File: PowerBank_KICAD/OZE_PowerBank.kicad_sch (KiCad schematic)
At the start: 62 parts, among them IC1 TPS2514ADBVT, J2 Conn_01x04_Pin, J3 USB_C_Receptacle_PowerOnly_6P, J4 USB_B_Micro, J5 Conn_01x04_Pin, J6 Conn_01x04_Pin, P1 USB_C_Plug_USB2.0, Q1 IRLZ44N, Q2 IRLZ44N, SW1 SW_SPDT, SW2 SW_Push, U1 INA180A2, U1 LM5106SD, U2 TLV70233_SOT23-5, U3 TPS25810RVCR, U4 STM32F103C8Tx, Y1 16MHz

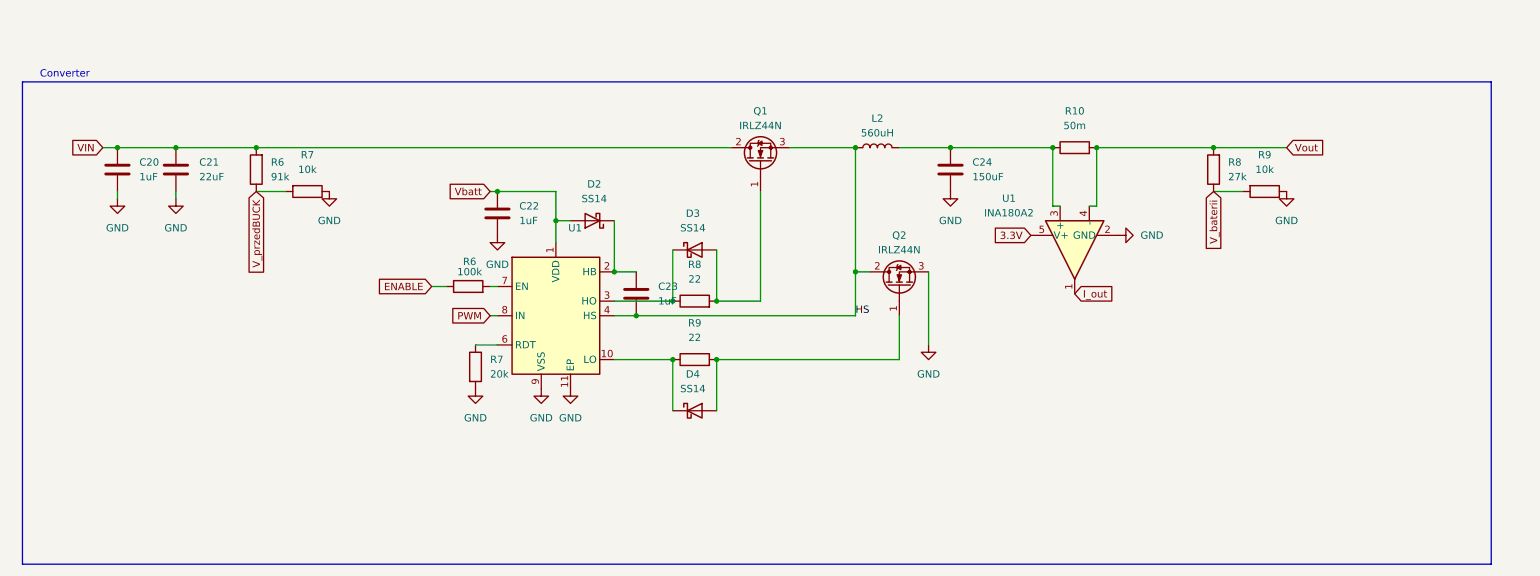
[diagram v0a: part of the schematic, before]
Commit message: 04.11
- 150uF kondensatory to elektrolity ważny LOW RMS!
- Przetwornica do sterownika (IMZ Przetwornica MT3608 2A Step-Up DC/DC) gotowa płytka
- 100 kHz sterowanie PWM (tak dobrany jest dławik i kondensatory co widać na symulacji)

Symulacja w LT Spice
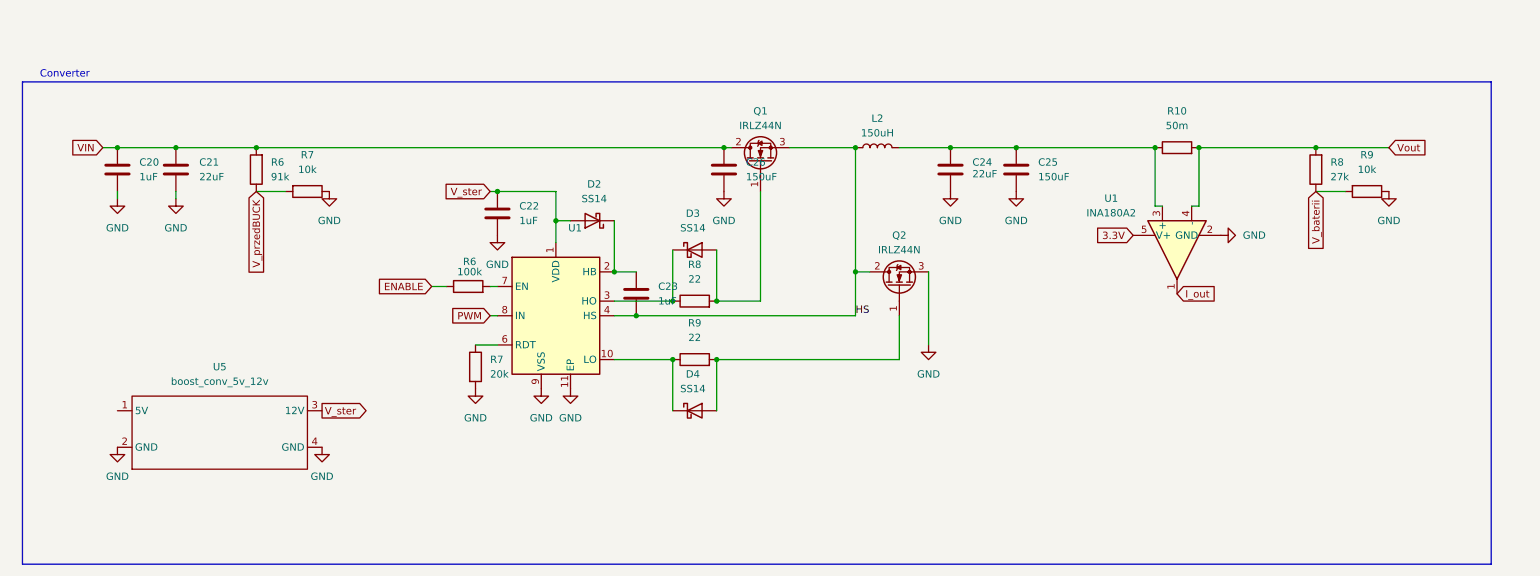
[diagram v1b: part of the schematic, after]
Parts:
- added C25, C26: 150uF, symbol Device:C
- added U5: boost_conv_5v_12v, symbol Biblioteka_PowerBank:boost_conv_5v_12v
- C24: value 150uF -> 22uF
- L2: value 560uH -> 150uH
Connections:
- net GND: now also C25.2, C26.2, U5.2 (GND), U5.4 (GND)
- net VIN: now also C26.1
- net at C24.1, L2.2, R10.1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: now also C25.1
- net Vbatt renamed V_ster
- net V_ster: now also U5.3 (12V)
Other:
- moved on the sheet: R10, R8, R9, U1

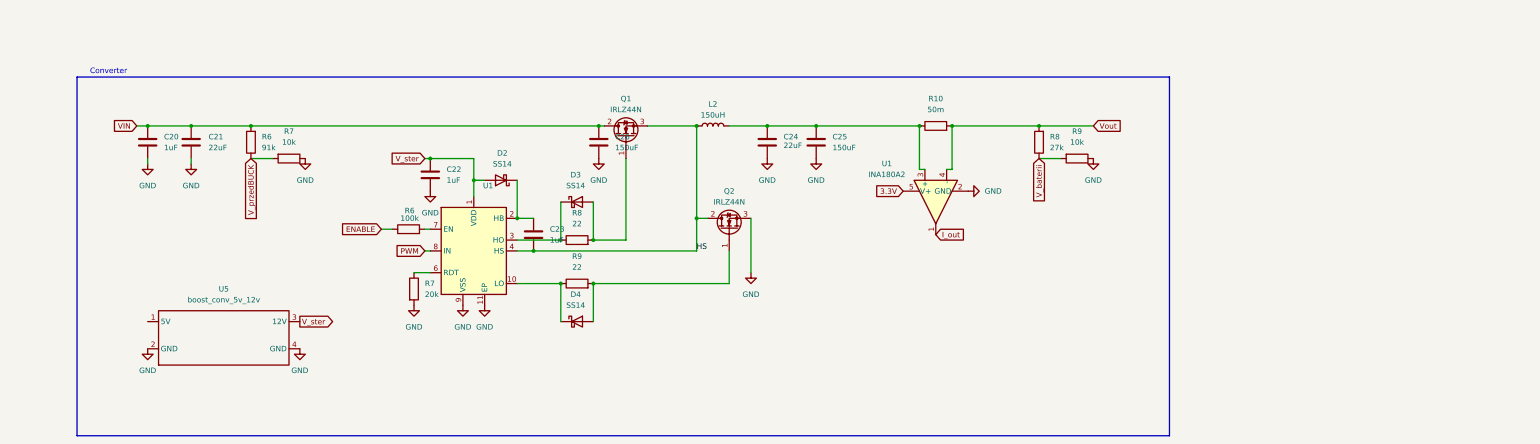
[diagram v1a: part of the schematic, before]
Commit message: BMS - 04.11 21:00 Hubert
Dodany BMS wraz z tranzystorem odcinającym masę dla układu ładowania
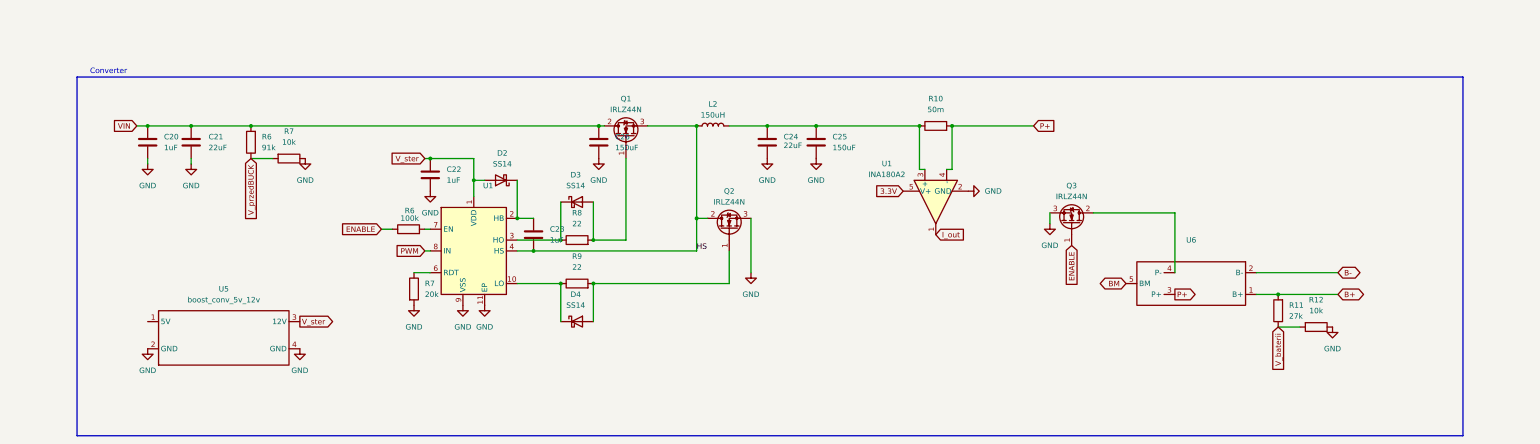
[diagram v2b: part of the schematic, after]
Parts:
- removed R8: 27k, symbol Device:R
- removed R9: 10k, symbol Device:R
- added Q3: IRLZ44N, Package_TO_SOT_THT:TO-220-3_Vertical, symbol Transistor_FET:IRLZ44N
- added R11: 27k, symbol Device:R
- added R12: 10k, symbol Device:R
- added U6: ~, symbol Biblioteka_PowerBank:BMS
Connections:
- net ENABLE: now also Q3.1 (G)
- net GND: now also Q3.3 (S), R12.1
- net V_baterii: now also R11.1, R12.2
- net Vout renamed P+
- net P+: now also U6.3 (P+)
- new net: Q3.2 (D), U6.4 (P-)
- new net B+: R11.2, U6.1 (B+)
- new net B-: U6.2 (B-)
- new net BM: U6.5 (BM)

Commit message: merge zmian
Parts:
- removed P1: USB_C_Plug_USB2.0, symbol Connector:USB_C_Plug_USB2.0
- added C1: 100n, Capacitor_SMD:C_0603_1608Metric_Pad1.08x0.95mm_HandSolder, symbol Device:C_Small
- added C7: 10uF, symbol Device:C_Small
- added D10, D11: SMAJ5.0CA, Diode_SMD:D_SMA, symbol Diode:SMAJ5.0CA
- added D5: SMBJ24CA, Diode_SMD:D_SMB, symbol Diode:1.5KExxCA
- added D6: 15V, Diode_SMD:D_MiniMELF, symbol Device:D_Zener
- added D7, D9: SS34, Diode_SMD:D_SMA, symbol Diode:SS34
- added F1: 1A, Fuse:Fuse_1812_4532Metric, symbol scorpio_Symbol_Library:BPT500_(PPTC)
- added J1: USB_A, symbol Connector:USB_A
- added J7, J8: Conn_01x02_Pin, symbol Connector:Conn_01x02_Pin
- added Q4: AO3407A, Package_TO_SOT_SMD:SOT-23_Handsoldering, symbol Device:Q_PMOS_GDS
- added R1: 10k, Resistor_SMD:R_0603_1608Metric, symbol Device:R_Small
- added U3: 74HC4051, symbol 74xx:74HC4051
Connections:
- net +3.3V: now also U3.16 (VCC); no longer SW2.1
- net CHG: now also U4.17 (PA7)
- net CHG_HI: now also U4.29 (PA8)
- net DM1: now also D10.1 (A1), J1.2 (D-); no longer J3.B5 (CC2)
- net DP1: now also D11.1 (A1), J1.3 (D+); no longer J3.A5 (CC1)
- net ENABLE: now also U4.10 (PA0)
- net GND: now also J3.A12 (GND), J3.B12 (GND), J3.S1 (SHIELD), SW2.1, U3.12 (GND), U3.21 (PAD), C1.2, C7.2, D10.2 (A2), D11.2 (A2), D5.1 (A1), J1.4 (GND), J1.5 (Shield), R1.1, U3.6 (~{E}), U3.7 (VEE), U3.8 (GND)
- net I_out: now also U3.12 (A3)
- net PWM: now also U4.11 (PA1)
- net VBUS: no longer C8.1, U2.1 (IN)
- net VIN: now also C8.1, U2.1 (IN), D6.1 (K), Q4.3 (S)
- net V_baterii: now also U3.14 (A1)
- net V_przedBUCK: now also U3.13 (A0)
- net at U3.11 (CC1): now also J3.B5 (CC2)
- net at U3.13 (CC2): now also J3.A5 (CC1)
- net at C10.1, C11.1, IC1.5 (IN)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: now also C7.1, J1.1 (VBUS)
- net S0: now reaches U4.14 (PA4)
- net S0: now also U3.11 (S0)
- net S1: now reaches U4.15 (PA5)
- net S1: now also U3.10 (S1)
- net S2: now reaches U4.16 (PA6)
- net S2: now also U3.9 (S2)
- net 5V renamed Vout
- net Vout: now also J7.1 (Pin_1), J8.1 (Pin_1), U3.15 (A2)
- new net: D5.2 (A2), F1.2, Q4.2 (D)
- new net: D6.2 (A), Q4.1 (G), R1.2
- new net COM OUT/IN: U3.3 (A)
- new net DC Charger: D9.2 (A)
- new net Packet-: J7.2 (Pin_2), J8.2 (Pin_2)
- new net Panel: D7.2 (A)
- new net Vpower: C1.1, D7.1 (K), D9.1 (K), F1.1
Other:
- note added: "5V power additional"
- note added: "Akumulator 2S, zabezpieczenie i ładowarka jednocześnie; wyprowadzamy tylko dwa piny + i -"
- note added: "Battery conection, BMS"
- note added: "CHG , CHG_HI set current capability"
- note added: "Check if PINS are compatible, PWM, ADC function assignment Add backup-pins in case of changing uC"
- note added: "DCP - dedicated charging point (bez hosta) do 2A"
- note added: "DFP"
- note added: "Do zasilania STM"
- note added: "JST XH footprint"
- note added: "NRST - ma pullup, więc musimy zewrzeć do masy dla resetu"
- note added: "Napięcia wejściowe uC max 3,3 V?"
- note added: "Nie potrzebne - Backup"
- note added: "OR Power - panel fotowoltaiczny, zasilacz DC, ładowarka USB (testy uC i programowanie)"
- note added: "PTC resetable fuse"
- note added: "Przeliczyć spadki napięcia, czy nie zadziała ochrona?"
- note added: "Reverse polarity and overcurrent protection"
- note added: "czy "-" i GND to będzie to samo?"
- note added: "czy zasilać bezpośrednio z panelu czy z ogniw"
- note added: "dodać złącze DC na płytce do podłączenia panelu, zasilacza"
- note added: "https://sklep.avt.pl/pl/products/modul-bms-pcm-pcb-ladowania-i-ochrony-ogniw-li-ion-2s-8-4v-13a-18650-183503.html?utm_source"
- note added: "jak zabezpieczyć żeby układ nie brał więcej niż 1 A jeżeli; z zasilacza?"
- note added: "przetwornica 8,4V -> 5V"
- moved on the sheet: 100k, C1, C10, C11, C12, C13, C14, C15, C16, C17, C18, C19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

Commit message: Update 05.11 19:00 - Hubert
Zmiany:
- oznaczenia zasilania na schemacie
- dodano przetwornice buck down
- dodano masę sygnałową ???
- po przemieszanie elementów na schemacie (czytelniej)
- zmiana kondensatorów odpowiednich na elektrolity (polarized)
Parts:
- removed C25, C26: 150uF, symbol Device:C
- removed Q3: IRLZ44N, Package_TO_SOT_THT:TO-220-3_Vertical, symbol Transistor_FET:IRLZ44N
- added C25, C27: 150uF, symbol Device:C_Polarized
- added C26: 22u, symbol Device:C_Small
- added C28: 22uF, symbol Device:C
- added U7: Przetwornica Buck Down na 5V, symbol Biblioteka_PowerBank:step_down_conv_8.4v_5v
- U6: value ~ -> BMS
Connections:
- net 3.3V is gone; now on net +3.3V: U1.5 (V+)
- net Packet- is gone; now on net GND: J7.2 (Pin_2), J8.2 (Pin_2)
- net B+: no longer R11.2
- net GND: now also U6.4 (P-), C25.2, C26.2, C27.2, C28.2, U7.2 (IN-), U7.4 (OUT-)
- net P+: now also J7.1 (Pin_1), J8.1 (Pin_1), R11.2, U3.15 (A2), C28.1, U7.1 (IN+)
- net VIN: now also C25.1; no longer C8.1, U2.1 (IN)
- net at C24.1, L2.2, R10.1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: now also C27.1
- net +5V: now reaches U5.1 (5V)
- net +5V: now also C14.1, C15.1, C8.1, U2.1 (IN), U3.2 (IN1), U3.3 (IN1), U3.4 (IN2), U3.5 (AUX), U3.6 (EN), C26.1, U7.3 (OUT+)
- net V_ster renamed +12V
- removed net Vout: C14.1, C15.1, J7.1 (Pin_1), J8.1 (Pin_1), U3.15 (A2), U3.2 (IN1), U3.3 (IN1), U3.4 (IN2), U3.5 (AUX), U3.6 (EN)
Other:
- moved on the sheet: 100k, C1, C10, C11, C12, C13, C14, C15, C16, C17, C18, C19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
